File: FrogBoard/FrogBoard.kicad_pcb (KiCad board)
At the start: 2 copper layers, 59.3 x 50.6 mm, 36 parts, among them J1 Conn_01x10, J2 Conn_01x04, J3 USB_B_Micro, J4 Stickbox, J5 Conn_01x03_Socket, U1 STM32L432KBUx, U2 USBLC6-2P6, U3 MCP1700T-3302E, U4 BL1555

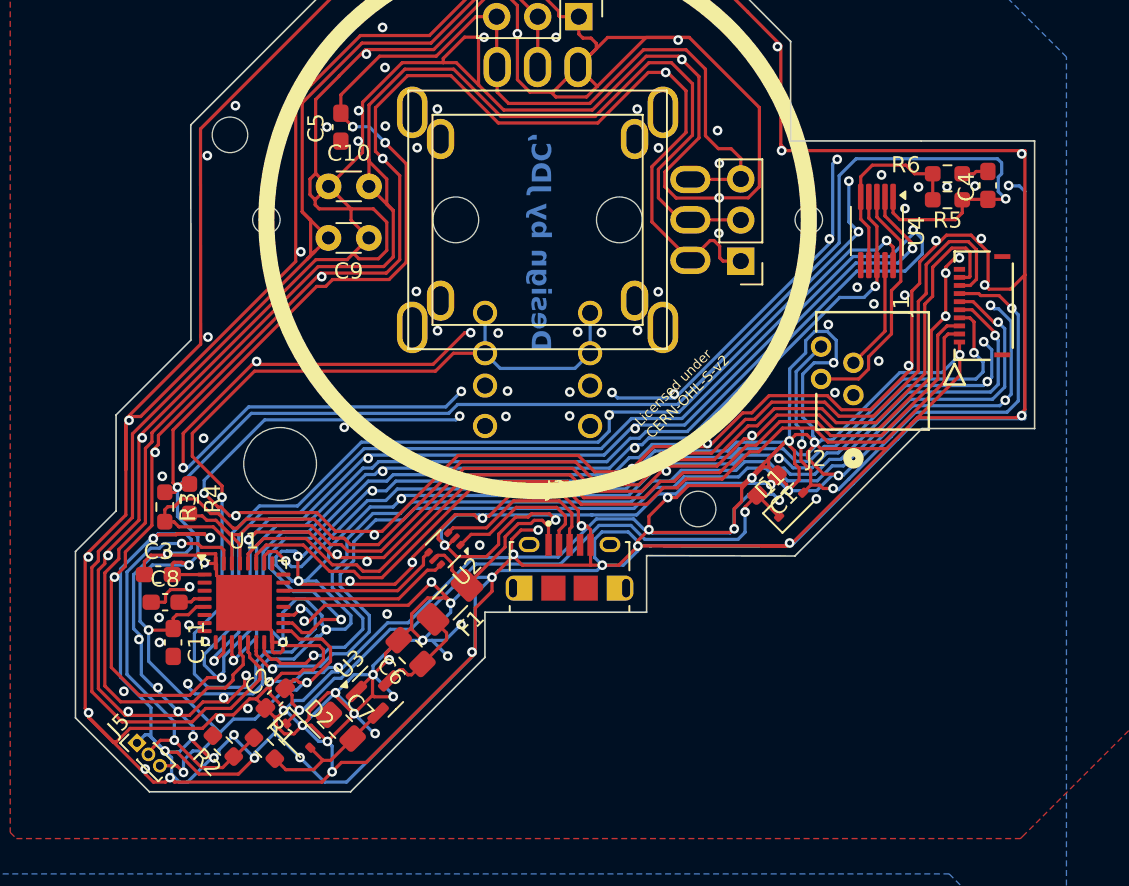
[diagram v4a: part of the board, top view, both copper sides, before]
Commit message: Add NRST header, clean up silkscreens
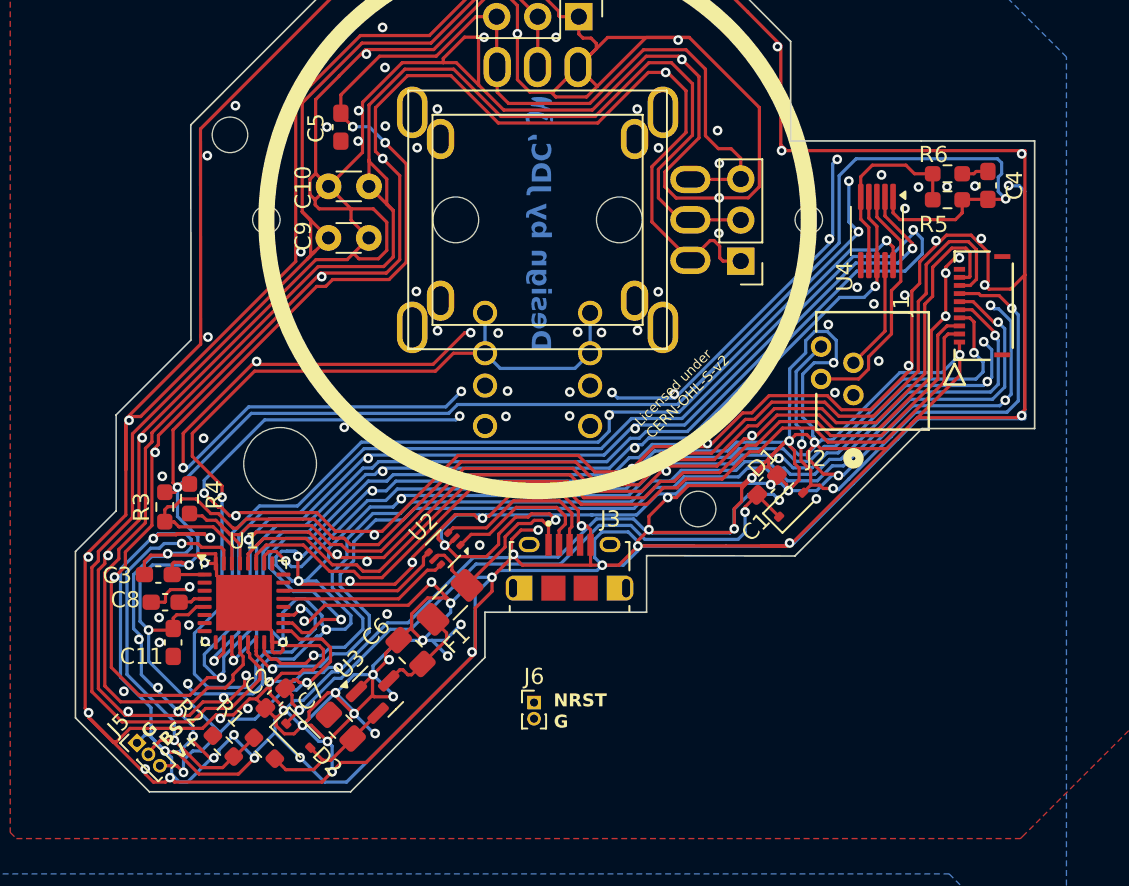
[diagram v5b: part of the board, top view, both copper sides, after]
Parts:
- added J6: Conn_01x02, Connector_PinHeader_1.00mm:PinHeader_1x02_P1.00mm_Vertical, F.Cu at (151.5, 119.1)
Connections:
- net Net-(U1-NRST) renamed NRST
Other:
- board text added: "BS"
- board text added: "G"
- board text added: "NRST"
- board text added: "V+"
- board text added: "X"
- board text added: "Y"

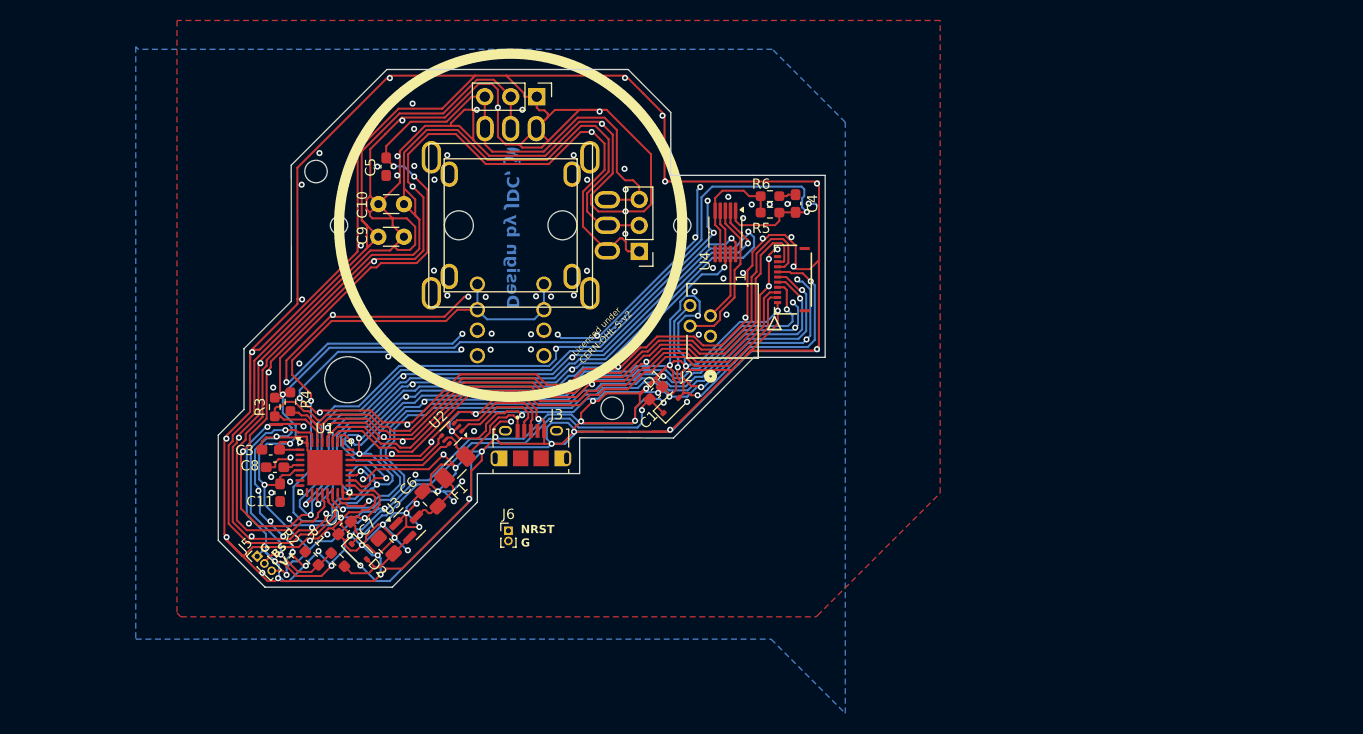
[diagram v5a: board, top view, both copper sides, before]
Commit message: Integrated reset header
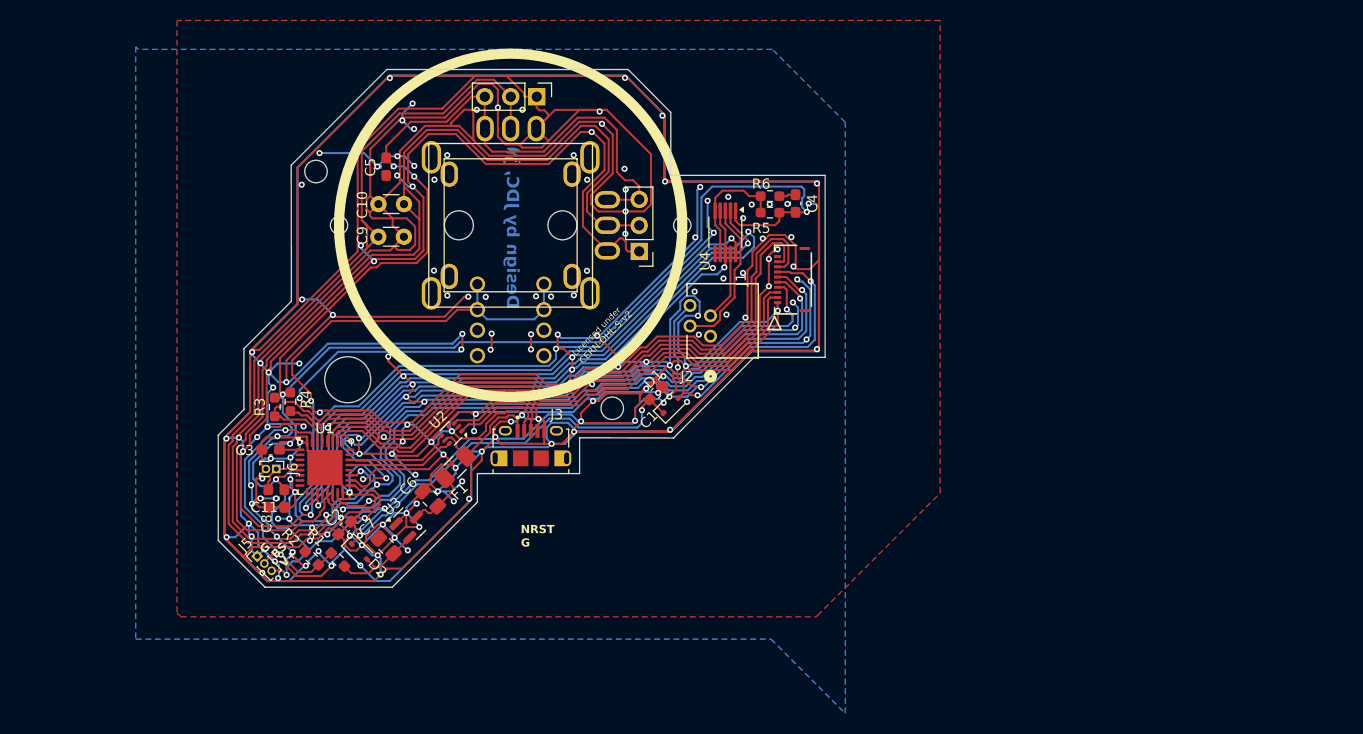
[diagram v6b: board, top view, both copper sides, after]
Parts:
- moved J6 23.5 mm to (128.8, 113.0), turned to -90 degrees
- moved C8 3.12 mm to (128.1, 115.9), turned to 90 degrees
- moved C11 0.70 mm to (129.6, 115.9)
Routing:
- net GND: track 1476.7 -> 1761.2 mm, vias 185 -> 189
- net +3.3V: track 242.0 -> 245.3 mm
- net NRST: track 1.64 -> 4.83 mm
- net AX_OUT: track 59.2 -> 59.8 mm

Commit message: Final board layout cleanup, added I2C testpoints
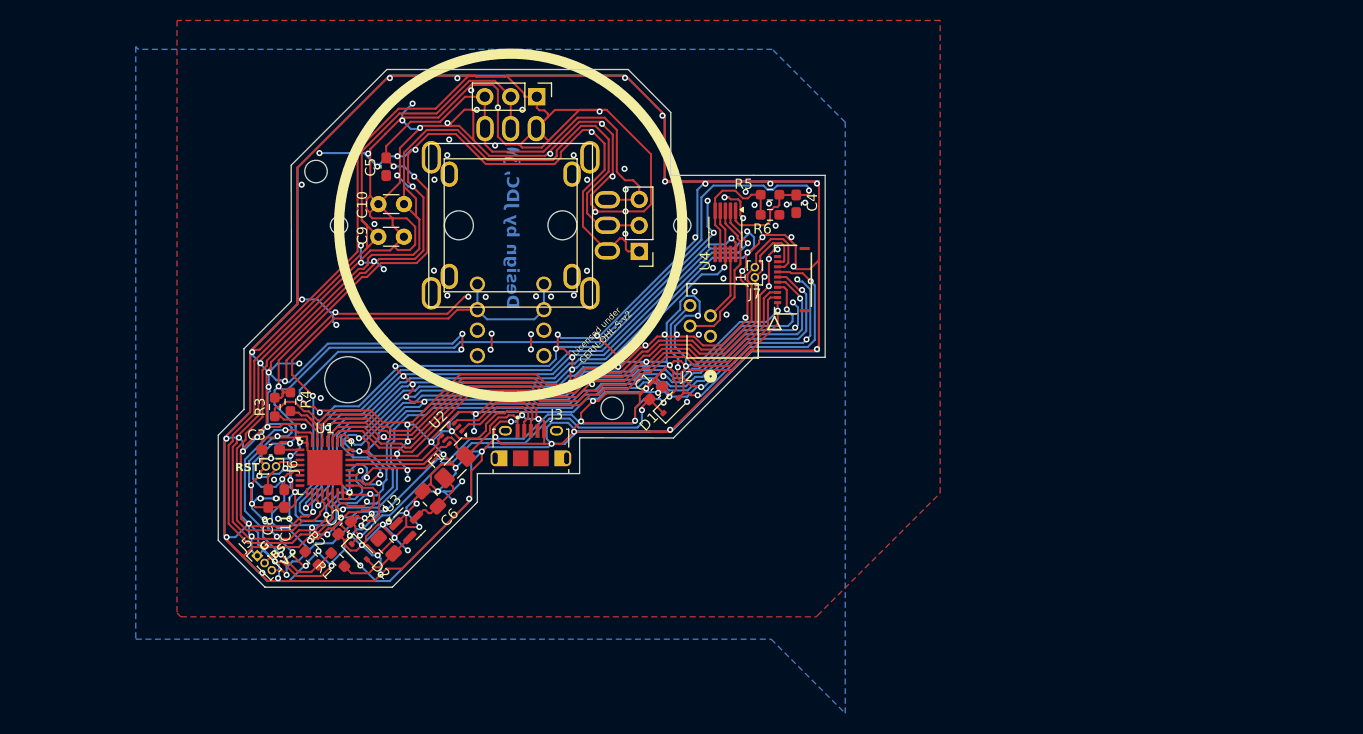
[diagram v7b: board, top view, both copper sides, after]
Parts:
- added J7: Conn_01x02, FrogBoard_footprints:PinHeader_1x02_P1.00mm_Vertical_Neutral_No_Coutryard, F.Cu at (175.6, 94.3)
- J6: footprint Connector_PinHeader_1.00mm:PinHeader_1x02_P1.00mm_Vertical -> FrogBoard_footprints:PinHeader_1x02_P1.00mm_Vertical_Neutral_No_Coutryard
- moved R6 1.83 mm to (177.1, 88.2)
- moved R5 1.75 mm to (177.1, 86.2)
- moved J6 0.25 mm to (128.8, 112.8)
- moved C4 0.07 mm to (179.7, 87.1), turned to 90 degrees
- moved J5 0.05 mm to (127.0, 121.5)
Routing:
- net GND: track 1761.2 -> 1778.2 mm, vias 189 -> 220
- net +3.3V: track 245.3 -> 247.8 mm
- net A_SEL: track 60.9 -> 59.7 mm
- net FFC_P6: track 67.7 -> 66.6 mm
- net FFC_P5: track 65.6 -> 64.6 mm
- net AY_IN: track 99.4 -> 100.1 mm
- net /A_MID: track 12.3 -> 12.8 mm
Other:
- board text added: "RST"
- board text added: "SDA"
- board text added: "SLC"
- board text removed: "NRST"

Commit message: Add part numbers, run DRC, add guide
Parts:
- U1: footprint Package_DFN_QFN:QFN-32-1EP_5x5mm_P0.5mm_EP3.45x3.45mm -> FrogBoard_footprints:QFN-32-1EP_5x5mm_P0.5mm_EP3.45x3.45mm
- U3: footprint Package_TO_SOT_SMD:SOT-23 -> FrogBoard_footprints:SOT-23
- U4: footprint Package_SO:MSOP-10_3x3mm_P0.5mm -> FrogBoard_footprints:MSOP-10_3x3mm_P0.5mm
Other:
- board text added: "FrogBoard v1.0.0-rc1"
